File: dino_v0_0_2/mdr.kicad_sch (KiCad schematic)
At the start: 16 parts, among them U18 74LS373, U22 74LS02, U25 74LS245, U34 74LS373, U37 74LS04, U39 74LS00, U72 74LS245, U73 74LS245

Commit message: feat: phase G_0 on silicon -- ROM readable as data, monitor runs its session
Three re-sourced pins make ROM readable as data (PROG_test3 0x4D, romsoak
0x00 over 65536 reads). The monitor then runs the session from the ask:
D 0000 -> 0x11, W FF00,99 -> 0x99, D FF00 -> 0x99, O FF00 on OB.

Four faults sat between the copper and that session, all fixed, all in
.git/sdd/PHASE_G_0.md RESULTS:

1. U15 (microcode EEPROM, CW8-15) pulsed END on its own for ~25ns with a
   static address, clean rails and ~OE/~CE low, locked to no clock in the
   machine. U61 turned it into ~MR low, U6 cleared T under HALT, and the
   byte behind the HALT ran. Every "HALT escape" ever recorded was this.
   Chip replaced; same image; no pulses.
2. MVI/MVIX/MVIS parked the immediate on a bus fight: CW14 flipped M to
   MAR before the source decode retired ~ROM_OUT, FETCH_RAM fired, and the
   RAM drove the cell's old byte under U18's open latch. PROG_isa was blind
   to it (PLANT rewrites the same 0x2E). Settle row with pc_up on the
   settle, not the park. Burned: U9 0xC52B  U15 0xDCD1  U23 0xCB8E.
3. LE_MDR opened on ~RAM_LOAD during the replay row. U39.4 strapped +5V;
   LE_MDR = NOT(READS_IDLE).
4. The spec's RAM-side wire (U74.9 <- READ) was identical logic and three
   gates faster on M15, which made fault 2 deterministic. Reverted to
   RAM_OE_ON.

Schematic matches copper: --since HEAD reads copper 3 (U22.11, U24.22,
U39.4), annotate 2; ERC delta -2, none new.

Tooling: asm/wander (ten slots, escape ladder), test4, test5 (six-slot
bisection), romsoak (ROM-as-data x65536, OB = misses), answer keys for
each; make gen-isa and burn-prog-isa; progrom_gen no longer writes over
asm-owned images; test_no_rom_park_flips_M_before_the_latch_closes.

OPEN: first ~3 data reads after POWER-UP miss, five witnesses in the doc.

Co-Authored-By: Claude Fable 5.1 <noreply@anthropic.com>
Claude-Session: https://claude.ai/code/session_01QTZogB99di5hEgzEycbhhD
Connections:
- net +5V: now also U39.4
- net READS_IDLE: now also U22.11
- net ~{RAM_LOAD}: no longer U39.4
- net ~{ROM_OUT}: no longer U22.11
- net READ: now reaches U37.1, U39.3
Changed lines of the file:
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@@
 	)
 	(junction
+		(at 45.72 48.26)
+		(diameter 0)
+		(color 0 0 0 0)
+	)
+	(junction
 		(at 132.08 72.39)
 		(diameter 0)
@@
 	(wire
 		(pts
+			(xy 27.94 63.5) (xy 27.94 66.04)
+		)
+		(stroke
+			(width 0)
+			(type default)
+		)
+	)
+	(wire
+		(pts
+			(xy 27.94 66.04) (xy 30.48 66.04)
+		)
+		(stroke
+			(width 0)
+			(type default)
+		)
+	)
+	(wire
+		(pts
+			(xy 134.62 198.12) (xy 138.43 198.12)
+		)
+		(stroke
+			(width 0)
+			(type default)
+		)
+	)
+	(wire
+		(pts
 			(xy 107.95 57.15) (xy 119.38 57.15)
 		)
@@
 	(wire
 		(pts
+			(xy 45.72 48.26) (xy 45.72 57.15)
+		)
+		(stroke
+			(width 0)
+			(type default)
+		)
+	)
+	(wire
+		(pts
 			(xy 137.16 114.3) (xy 144.78 114.3)
 		)
@@
 	(wire
 		(pts
+			(xy 45.72 57.15) (xy 53.34 57.15)
+		)
+		(stroke
+			(width 0)
+			(type default)
+		)
+	)
+	(wire
+		(pts
 			(xy 190.5 46.99) (xy 196.85 46.99)
 		)
@@
 		)
 	)
-	(wire
-		(pts
-			(xy 134.62 198.12) (xy 138.43 198.12)
-		)
-		(stroke
-			(width 0)
-			(type default)
-		)
-	)
 	(bus
 		(pts
@@
 		)
 	)
+	(label "RAM_OE_ON"
+		(at 138.43 198.12 0)
+		(effects
+			(font
+				(size 1.27 1.27)
+			)
+			(justify left bottom)
+		)
+	)
 	(label "PC12"
 		(at 246.38 121.92 0)
@@
 		)
 	)
-	(label "~{ROM_OUT}"
-		(at 25.4 185.42 180)
-		(effects
-			(font
-				(size 1.27 1.27)
-			)
-			(justify right bottom)
-		)
-	)
 	(label "PC3"
 		(at 246.38 63.5 0)
@@
 		)
 	)
-	(label "~{RAM_LOAD}"
-		(at 30.48 66.04 180)
-		(effects
-			(font
-				(size 1.27 1.27)
-			)
-			(justify right bottom)
-		)
-	)
 	(label "PC0"
 		(at 246.38 55.88 0)
@@
 		)
 	)
-	(label "RAM_OE_ON"
-		(at 138.43 198.12 0)
-		(effects
-			(font
-				(size 1.27 1.27)
-			)
-			(justify left bottom)
-		)
-	)
 	(label "W7"
 		(at 107.95 57.15 0)
@@
 		)
 	)
+	(label "READ"
+		(at 53.34 57.15 0)
+		(effects
+			(font
+				(size 1.27 1.27)
+			)
+			(justify left bottom)
+		)
+	)
 	(label "MDR6"
 		(at 157.48 54.61 0)
@@
 		)
 	)
+	(label "READS_IDLE"
+		(at 25.4 185.42 180)
+		(effects
+			(font
+				(size 1.27 1.27)
+			)
+			(justify right bottom)
+		)
+	)
 	(label "MDR5"
 		(at 214.63 68.58 0)
@@
 		)
 	)
+	(symbol
+		(lib_id "power:+5V")
+		(at 27.94 63.5 0)
+		(unit 1)
+		(body_style 1)
+		(exclude_from_sim no)
+		(in_bom yes)
+		(on_board yes)
+		(in_pos_files yes)
+		(dnp no)
+		(fields_autoplaced yes)
+		(property "Reference" "#PWR0226"
+			(at 27.94 67.31 0)
+			(hide yes)
+			(show_name no)
+			(do_not_autoplace no)
+			(effects
+				(font
+					(size 1.27 1.27)
+				)
+			)
+		)
+		(property "Value" "+5V"
+			(at 27.94 58.42 0)
+			(show_name no)
+			(do_not_autoplace no)
+			(effects
+				(font
+					(size 1.27 1.27)
+				)
+			)
+		)
+		(property "Footprint" ""
+			(at 27.94 63.5 0)
+			(hide yes)
+			(show_name no)
+			(do_not_autoplace no)
+			(effects
+				(font
+					(size 1.27 1.27)
+				)
+			)
+		)
+		(property "Datasheet" ""
+			(at 27.94 63.5 0)
+			(hide yes)
+			(show_name no)
+			(do_not_autoplace no)
+			(effects
+				(font
+					(size 1.27 1.27)
+				)
+			)
+		)
+		(property "Description" "Power symbol creates a global label with name \"+5V\""
+			(at 27.94 63.5 0)
+			(hide yes)
+			(show_name no)
+			(do_not_autoplace no)
+			(effects
+				(font
+					(size 1.27 1.27)
+				)
+			)
+		)
+		(pin "1"
+		)
+		(instances
+			(project "dino_v0_0_2"
+				(path "/e43166a5-d972-471d-b3cf-9f4f12c7f541/dfdf99e6-2845-4ba5-89ea-a5852382fb95"
+					(reference "#PWR0226")
+					(unit 1)
+				)
+			)
+		)
+	)

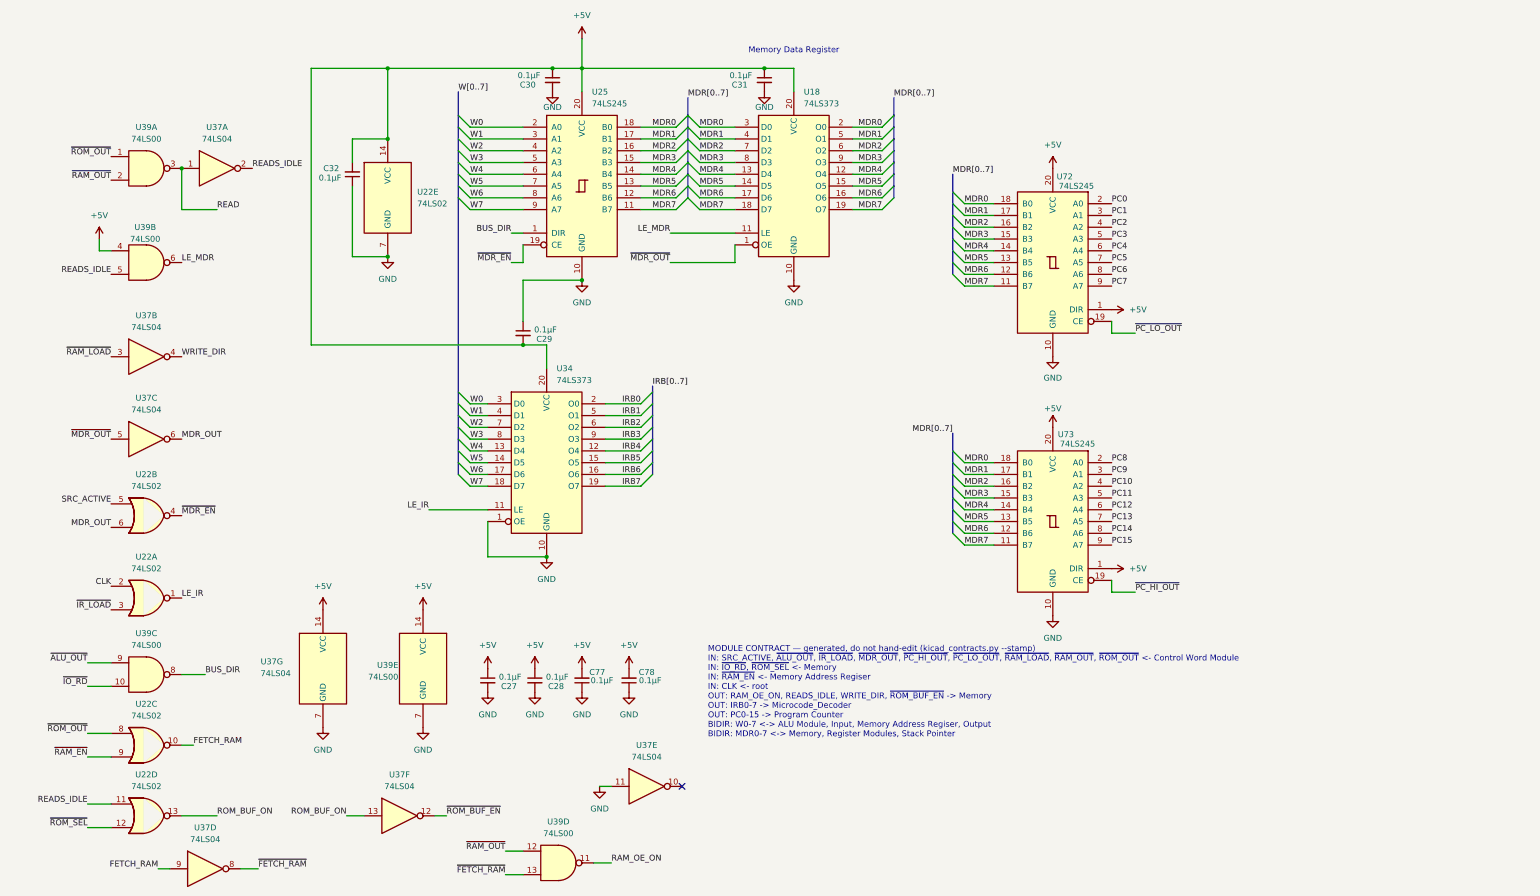
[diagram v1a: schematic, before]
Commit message: feat(kicad): footprints, power sheet, global labels, PCB draft
Every symbol gets a stock THT footprint (plain DIP, no sockets, so the
3D render shows ICs). New Power sheet: 24-pin ATX header for a picoPSU,
rails +5V/+3.3V/+12V/-12V/GND only; no -5V exists on any ATX unit since
2003, none drawn. PS_ON# on a 2-pin header.

Cross-sheet labels become global labels. KiCad joined nothing between
sheets before: 122 base names were split per sheet, ERC saw 90 undriven
inputs whose driver sat one sheet away, and the PCB ratsnest stopped at
every sheet boundary. Proof: KiCad's netlist after equals a name-join of
its netlist before plus the 15 CW alias pairs, pin for pin.

kicad_contracts took a node's sheet from the net name's /Sheet/ prefix;
global nets have none, so it emitted an empty contracts doc. Sheet now
comes from the component's own path; the doc regenerates with zero diff.

ERC 477 -> 2. Real fixes: ROM I/O pins input -> tri_state, '382 GND pin
power_out -> power_in, four orphan symbols rehomed to project lib `dino`,
one stub wire. 133 by-design warnings excluded by uuid ('245 readback on
counter Q, alias stubs, probe-point labels); the two left are bus
signals the peripheral bus sheet will consume.

PCB draft: 198 footprints placed per sheet, all pads netted, no tracks.

Co-Authored-By: Claude Fable 5.1 <noreply@anthropic.com>
Claude-Session: https://claude.ai/code/session_018irreFHb1xEykW5kCD26ow
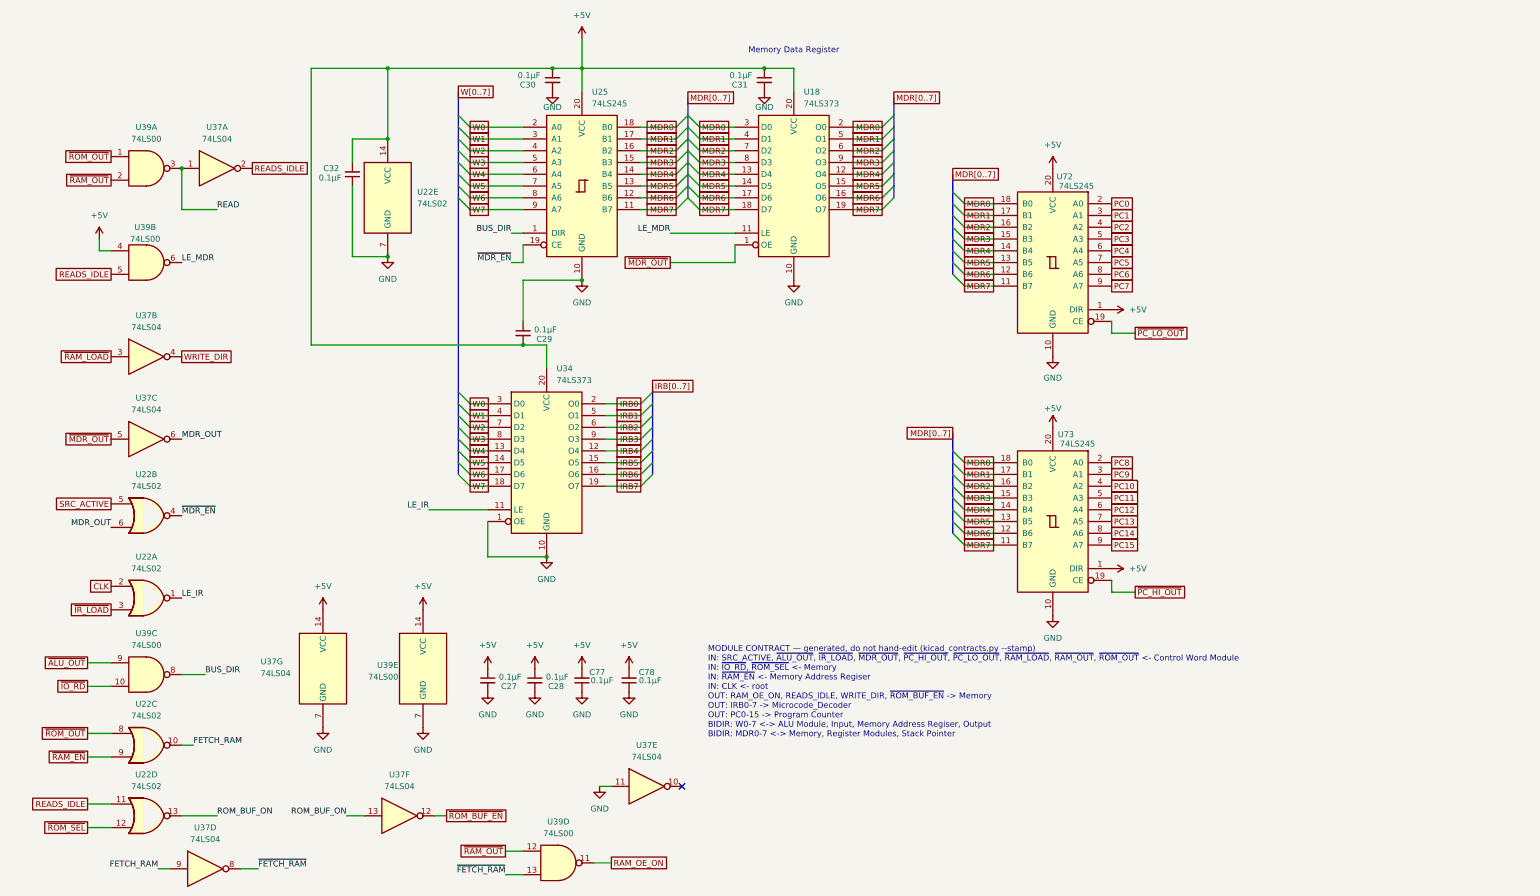
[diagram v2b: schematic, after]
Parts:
- C27, C28, C29, C30, C31, C32, C77, C78: footprint (none) -> Capacitor_THT:C_Disc_D5.0mm_W2.5mm_P2.50mm
- U18, U25, U34, U72, U73: footprint (none) -> Package_DIP:DIP-20_W7.62mm
- U22, U37, U39: footprint (none) -> Package_DIP:DIP-14_W7.62mm
